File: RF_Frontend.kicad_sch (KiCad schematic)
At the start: 52 parts, among them IC2 SX1280, U11 SC4215ASTRT, U12 SKY66112-11, U13 DEA202450BT-1213C1, Y3 Crystal_GND24

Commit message: Changed uart conn
Get transposed!
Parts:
- added RADIO_D_JP1: j, Jumper:SolderJumper-2_P1.3mm_Open_RoundedPad1.0x1.5mm, symbol Jumper:Jumper_2_Small_Bridged
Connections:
- net VS: now also RADIO_D_JP1.2 (B); no longer C54.1, IC2.11 (VBAT_IO)
- new net: C54.1, IC2.11 (VBAT_IO), RADIO_D_JP1.1 (A)
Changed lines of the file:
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@@
 	(wire
 		(pts
+			(xy 99.06 95.25) (xy 101.6 95.25)
+		)
+		(stroke
+			(width 0)
+			(type default)
+		)
+	)
+	(wire
+		(pts
 			(xy 227.33 76.2) (xy 227.33 78.74)
 		)
@@
 	(wire
 		(pts
-			(xy 86.36 95.25) (xy 90.17 95.25)
+			(xy 86.36 95.25) (xy 93.98 95.25)
 		)
 		(stroke
@@
 	)
 	(symbol
+		(lib_id "Jumper:Jumper_2_Small_Bridged")
+		(at 96.52 95.25 0)
+		(unit 1)
+		(exclude_from_sim yes)
+		(in_bom yes)
+		(on_board yes)
+		(dnp no)
+		(property "Reference" "RADIO_D_JP1"
+			(at 96.52 89.662 0)
+			(effects
+				(font
+					(size 1.27 1.27)
+				)
+			)
+		)
+		(property "Value" "j"
+			(at 96.774 97.282 0)
+			(effects
+				(font
+					(size 1.27 1.27)
+				)
+			)
+		)
+		(property "Footprint" "Jumper:SolderJumper-2_P1.3mm_Open_RoundedPad1.0x1.5mm"
+			(at 96.52 95.25 0)
+			(effects
+				(font
+					(size 1.27 1.27)
+				)
+				(hide yes)
+			)
+		)
+		(property "Datasheet" "~"
+			(at 96.52 95.25 0)
+			(effects
+				(font
+					(size 1.27 1.27)
+				)
+				(hide yes)
+			)
+		)
+		(property "Description" "Jumper, 2-pole, small symbol, bridged"
+			(at 96.52 95.25 0)
+			(effects
+				(font
+					(size 1.27 1.27)
+				)
+				(hide yes)
+			)
+		)
+		(pin "1"
+		)
+		(pin "2"
+		)
+		(instances
+			(project ""
+				(path "/7db990e4-92e1-4f99-b4d2-435bbec1ba83/ecfc1314-a0cb-4bac-a35c-d2175f1c7197"
+					(reference "RADIO_D_JP1")
+					(unit 1)
+				)
+			)
+		)
+	)
+	(symbol
 		(lib_id "Connector:TestPoint")
 		(at 67.31 142.24 90)
@@
 	(symbol
 		(lib_id "power:VS")
-		(at 90.17 95.25 0)
+		(at 101.6 95.25 0)
 		(unit 1)
 		(exclude_from_sim no)
@@
 		(dnp no)
 		(property "Reference" "#PWR085"
-			(at 90.17 99.06 0)
+			(at 101.6 99.06 0)
 			(effects
 				(font
@@
 		)
 		(property "Value" "VS"
-			(at 92.71 93.98 0)
+			(at 104.14 93.98 0)
 			(effects
 				(font
@@
 		)
 		(property "Footprint" ""
-			(at 90.17 95.25 0)
+			(at 101.6 95.25 0)
 			(effects
 				(font
@@
 		)
 		(property "Datasheet" ""
-			(at 90.17 95.25 0)
+			(at 101.6 95.25 0)
 			(effects
 				(font
@@
 		)
 		(property "Description" "Power symbol creates a global label with name \"VS\""
-			(at 90.17 95.25 0)
+			(at 101.6 95.25 0)
 			(effects
 				(font

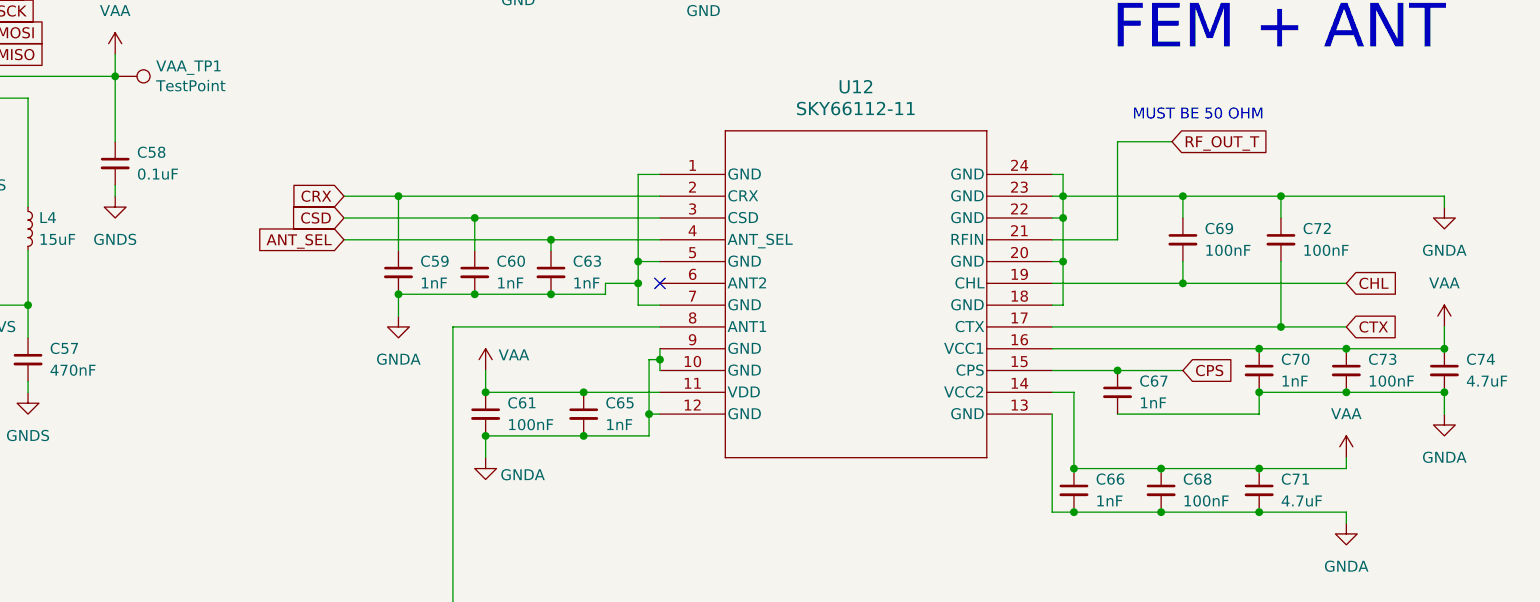
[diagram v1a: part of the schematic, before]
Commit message: Changed via stitching
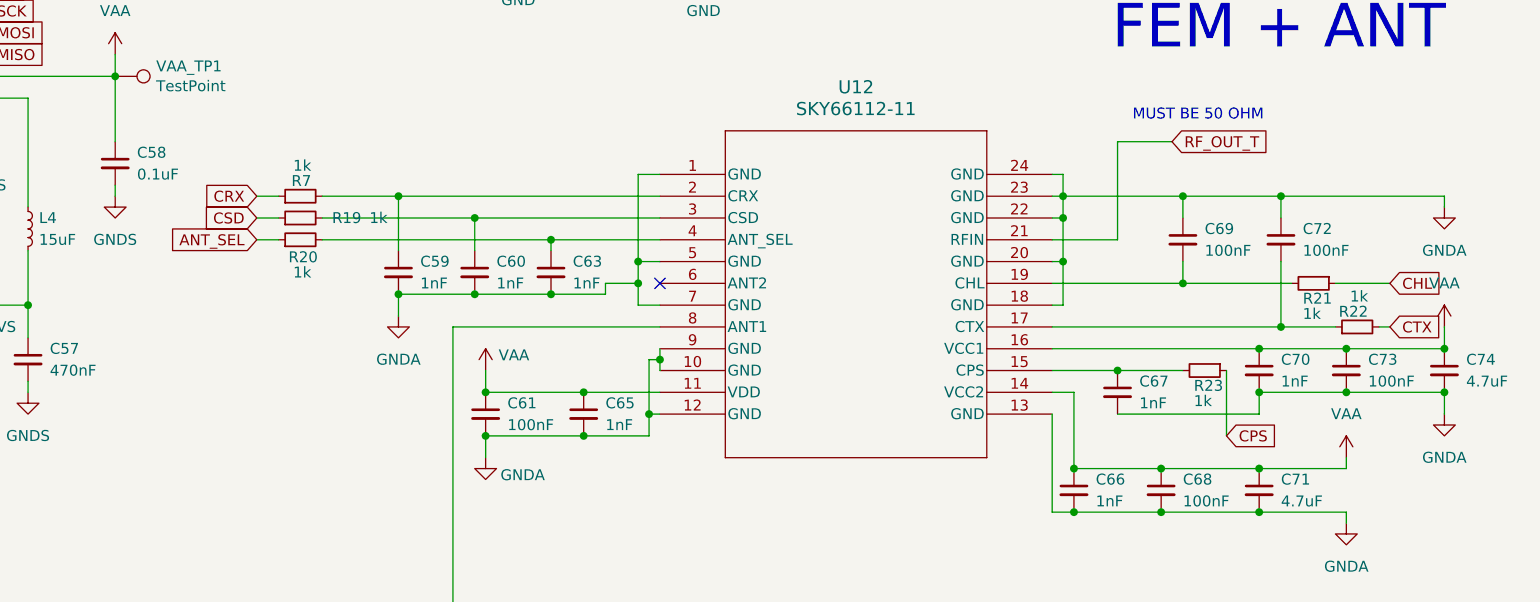
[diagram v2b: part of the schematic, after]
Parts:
- added R19, R20, R21, R22, R23, R7: 1k, Resistor_SMD:R_0402_1005Metric, symbol Device:R_Small
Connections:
- net ANT_SEL: now also R20.1; no longer C63.1, U12.4 (ANT_SEL)
- net CHL: now also R21.1; no longer C69.2, U12.19 (CHL)
- net CPS: now also R23.1; no longer C67.1, U12.15 (CPS)
- net CRX: now also R7.1; no longer C59.1, U12.2 (CRX)
- net CSD: now also R19.1; no longer C60.1, U12.3 (CSD)
- net CTX: now also R22.2; no longer C72.2, U12.17 (CTX)
- new net: C69.2, R21.2, U12.19 (CHL)
- new net: C59.1, R7.2, U12.2 (CRX)
- new net: C63.1, R20.2, U12.4 (ANT_SEL)
- new net: C72.2, R22.1, U12.17 (CTX)
- new net: C67.1, R23.2, U12.15 (CPS)
- new net: C60.1, R19.2, U12.3 (CSD)

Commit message: Minor improvements
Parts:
- added R31, R32, R33, R34: 20-100, Resistor_SMD:R_0402_1005Metric, symbol Device:R_Small
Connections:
- net CS: now also R31.1; no longer IC2.19 (NSS_CTS)
- net MISO: now also R34.1; no longer IC2.16 (MISO_TX)
- net MOSI: now also R33.1; no longer IC2.17 (MOSI_RX)
- net SCK: now also R32.1; no longer IC2.18 (SCK_RTSN)
- new net: IC2.16 (MISO_TX), R34.2
- new net: IC2.17 (MOSI_RX), R33.2
- new net: IC2.18 (SCK_RTSN), R32.2
- new net: IC2.19 (NSS_CTS), R31.2
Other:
- note added: "I'm not smart enough to know when to split or not split grounds"
- note removed: "Splitting grounds is a dumb idea 99.98% of the time."
- moved on the sheet: ANT1, ANT_S1, BUSY1, C12, C18, C19, C50, C51, C52, C53, C54, C57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

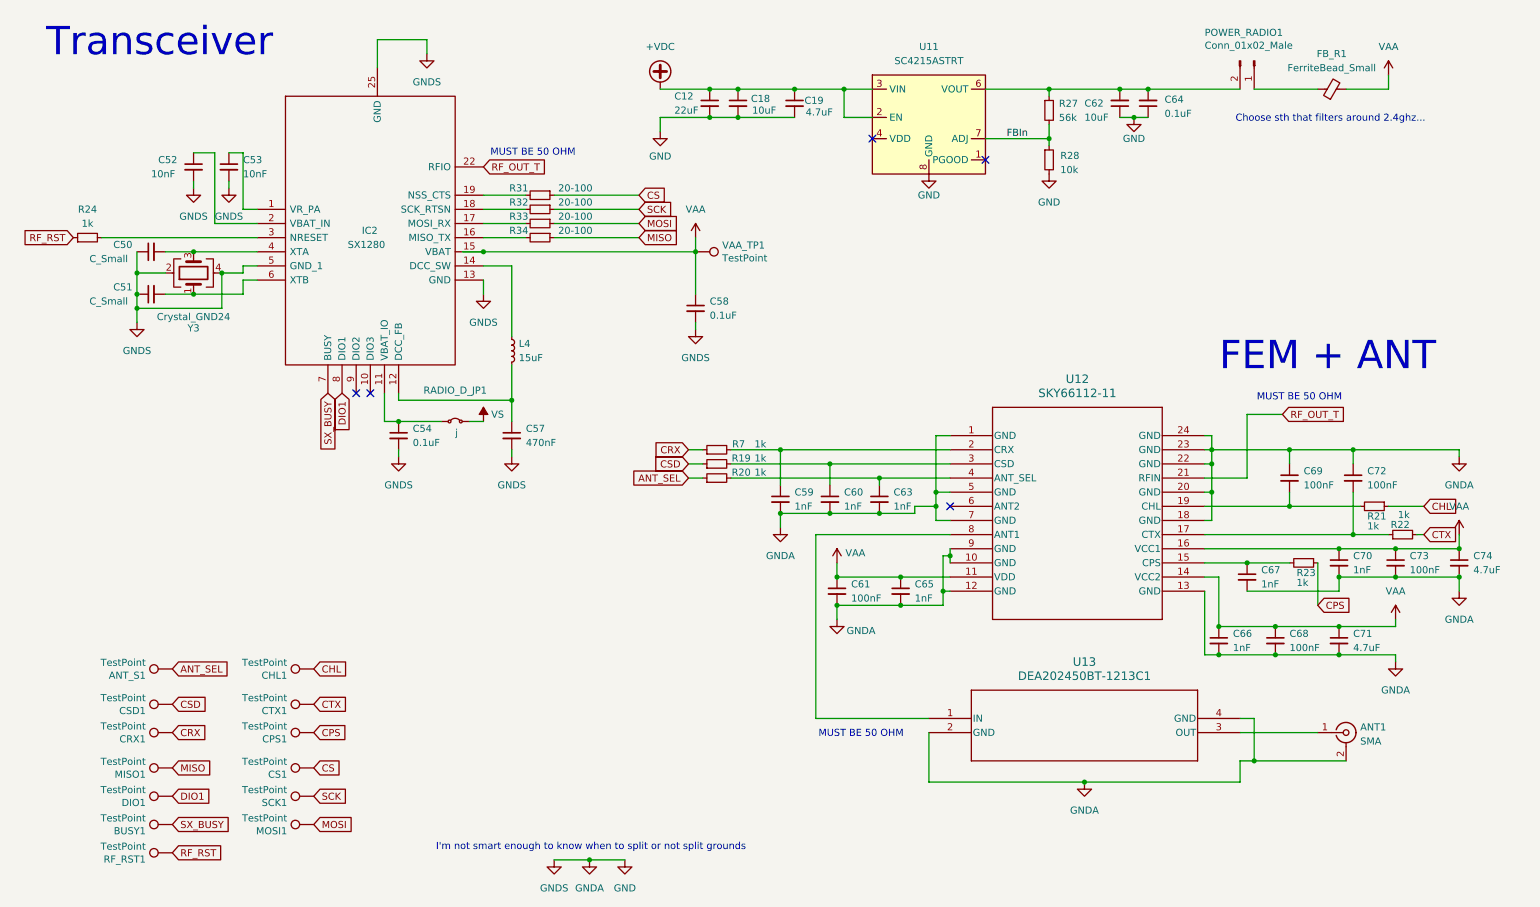
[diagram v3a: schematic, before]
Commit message: Fixed Libraries
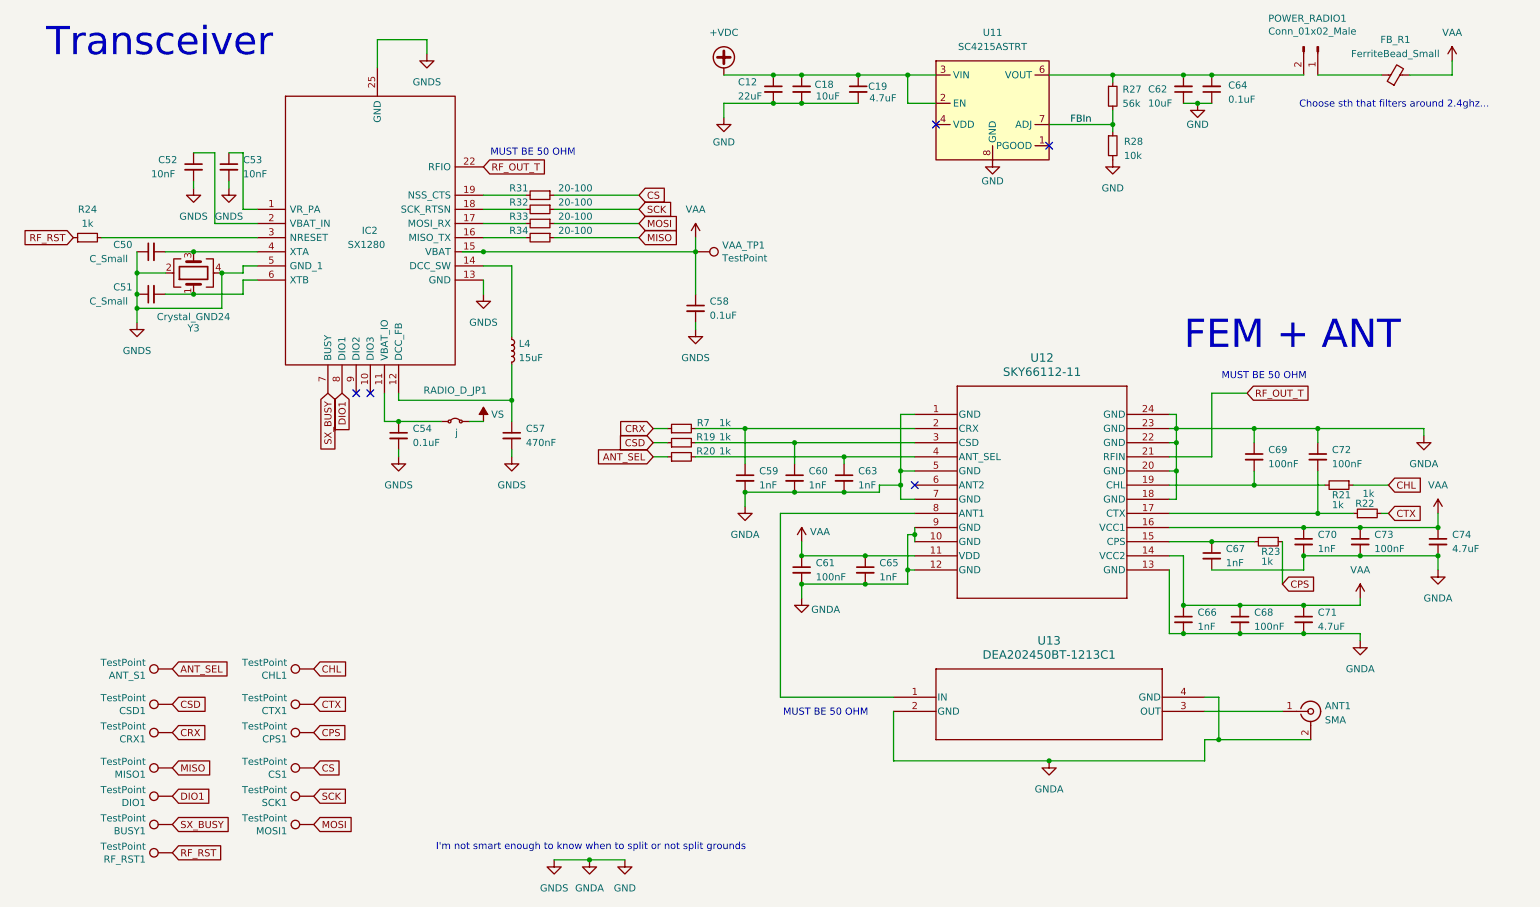
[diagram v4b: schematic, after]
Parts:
- IC2: footprint footprints:QFN50P400X400X95-24N -> iclr:QFN50P400X400X95-24N
- U11: footprint footprints:SOIC127P599X175-9N -> iclr:SOIC127P599X175-9N
- U12: footprint footprints:SKY66112-11_SKY -> iclr:SKY66112-11_SKY; symbol SKYRF:SKY66112-11 -> iclr:SKY66112-11
- U13: footprint footprints:DEA-4_2P0X1P25 -> iclr:DEA-4_2P0X1P25; symbol 2024-11-05_19-33-17:DEA202450BT-1213C1 -> iclr:DEA202450BT-1213C1
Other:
- moved on the sheet: ANT1, C12, C18, C19, C59, C60, C61, C62, C63, C64, C65, C66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

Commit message: Post review changes WIP
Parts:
- removed C59, C60, C63, C67: 1nF, Capacitor_SMD:C_0402_1005Metric, symbol Device:C_Small
- removed C69, C72: 100nF, Capacitor_SMD:C_0402_1005Metric, symbol Device:C_Small
- removed POWER_RADIO1: Conn_01x02_Male, Connector_PinHeader_2.54mm:PinHeader_1x02_P2.54mm_Vertical, symbol Connector:Conn_01x02_Male
- removed R19, R20, R21, R22, R23, R24, R7: 1k, Resistor_SMD:R_0402_1005Metric, symbol Device:R_Small
- removed RADIO_D_JP1: j, Jumper:SolderJumper-2_P1.3mm_Open_RoundedPad1.0x1.5mm, symbol Jumper:Jumper_2_Small_Bridged
- added ANT2: u.FL, Connector_Coaxial:U.FL_Hirose_U.FL-R-SMT-1_Vertical, symbol Connector:Conn_Coaxial
- added DIO2, DIO3: TestPoint, TestPoint:TestPoint_Pad_D1.0mm, symbol Connector:TestPoint
- added J3: Conn_01x03_Pin, Connector_PinHeader_2.54mm:PinHeader_1x03_P2.54mm_Vertical, symbol Connector:Conn_01x03_Pin
- added R35: 0, Resistor_SMD:R_0402_1005Metric, symbol Device:R_Small
- added R36, R37, R38: 470, Resistor_SMD:R_0402_1005Metric, symbol Device:R_Small
- added TXLED2, TXLED3, TXLED4: GREEN_LED, Resistor_SMD:R_0402_1005Metric, symbol Device:LED_Small
- added U6: DEA202450BT-1213C1, iclr:DEA-4_2P0X1P25, symbol iclr:DEA202450BT-1213C1
- L4: value 15uF -> 15uH
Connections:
- net ANT_SEL: now also U12.4 (ANT_SEL)
- net CHL: now also U12.19 (CHL)
- net CPS: now also U12.15 (CPS)
- net CRX: now also U12.2 (CRX)
- net CSD: now also U12.3 (CSD)
- net CTX: now also U12.17 (CTX)
- net DIO1: now also R36.1
- net GND: now also ANT2.2 (Ext), TXLED2.1 (K), TXLED3.1 (K), TXLED4.1 (K), U6.2 (GND), U6.4 (GND)
- net RF_RST: now also IC2.3 (NRESET)
- net VAA: now also C53.1, IC2.1 (VR_PA)
- net VS: now also R35.2
- net at FB_R1.1: now also J3.1 (Pin_1), J3.2 (Pin_2)
- net at C62.2, C64.2, R27.1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: now also J3.3 (Pin_3)
- net VDDF: now reaches C57.1, IC2.12 (DCC_FB), L4.2
- net VDDF: now also C52.1, C54.1, IC2.11 (VBAT_IO), IC2.2 (VBAT_IN), R35.1
- net DIO3: now reaches IC2.10 (DIO3)
- net DIO3: now also DIO3.1, R38.1
- net DIO2: now reaches IC2.9 (DIO2)
- net DIO2: now also DIO2.1, R37.1
- net at U12.6 (ANT2): now also U6.1 (IN)
- new net: R38.2, TXLED4.2 (A)
- new net: ANT2.1 (In), U6.3 (OUT)
- new net: R37.2, TXLED3.2 (A)
- new net: R36.2, TXLED2.2 (A)
- no-connect marks 5 -> 2
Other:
- moved on the sheet: BUSY1, C54, RF_RST1

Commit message: Minor fixes
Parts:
- renumbered TXLED4 to DIO3_D1, TXLED3 to RXD_1, TXLED2 to TXD_1
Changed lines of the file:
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@@
 		(on_board yes)
 		(dnp no)
-		(property "Reference" "TXLED3"
+		(property "Reference" "RXD_1"
 			(at 107.95 143.637 0)
 			(effects
@@
 			(project "Ricardo-Hermes"
 				(path "/7db990e4-92e1-4f99-b4d2-435bbec1ba83/ecfc1314-a0cb-4bac-a35c-d2175f1c7197"
-					(reference "TXLED3")
+					(reference "RXD_1")
 					(unit 1)
 				)
@@
 		(on_board yes)
 		(dnp no)
-		(property "Reference" "TXLED4"
+		(property "Reference" "DIO3_D1"
 			(at 107.95 153.797 0)
 			(effects
@@
 			(project "Ricardo-Hermes"
 				(path "/7db990e4-92e1-4f99-b4d2-435bbec1ba83/ecfc1314-a0cb-4bac-a35c-d2175f1c7197"
-					(reference "TXLED4")
+					(reference "DIO3_D1")
 					(unit 1)
 				)
@@
 		(on_board yes)
 		(dnp no)
-		(property "Reference" "TXLED2"
+		(property "Reference" "TXD_1"
 			(at 107.95 133.477 0)
 			(effects
@@
 			(project "Ricardo-Hermes"
 				(path "/7db990e4-92e1-4f99-b4d2-435bbec1ba83/ecfc1314-a0cb-4bac-a35c-d2175f1c7197"
-					(reference "TXLED2")
+					(reference "TXD_1")
 					(unit 1)
 				)

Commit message: Silkscreen WIP
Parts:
- R35: footprint Resistor_SMD:R_0402_1005Metric -> Resistor_SMD:R_0603_1608Metric
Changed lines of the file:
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@@
 			)
 		)
-		(property "Footprint" "Resistor_SMD:R_0402_1005Metric"
+		(property "Footprint" "Resistor_SMD:R_0603_1608Metric"
 			(at 93.98 109.22 0)
 			(effects

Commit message: Post Review changes, more to come...
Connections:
- net CHL: now also CTX1.1; no longer CHL1.1
- net CTX: now also CHL1.1; no longer CTX1.1
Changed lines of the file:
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@@
 	(global_label "CHL"
 		(shape input)
-		(at 68.58 138.43 0)
+		(at 68.58 144.78 0)
 		(fields_autoplaced yes)
 		(effects
@@
 		)
 		(property "Intersheetrefs" "${INTERSHEET_REFS}"
-			(at 74.5396 138.43 0)
+			(at 74.5396 144.78 0)
 			(effects
 				(font
@@
 	(global_label "CTX"
 		(shape input)
-		(at 68.58 144.78 0)
+		(at 68.58 138.43 0)
 		(fields_autoplaced yes)
 		(effects
@@
 		)
 		(property "Intersheetrefs" "${INTERSHEET_REFS}"
-			(at 74.3581 144.78 0)
+			(at 74.3581 138.43 0)
 			(effects
 				(font
